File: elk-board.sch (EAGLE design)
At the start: 199 parts, among them IC1 KLM8G1GESD-B03P, IC10 MP2143DJ-LF-P, IC2 ALLWINNER--H3, IC3 SY6280, IC4 K4B4G1646D-BCK0, IC5 RT8059GJ5, IC6 RT8059GJ5, IC7 SY8089A, IC8 NCP803SN263T1G, IC9 RT8059GJ5, Q1 AO3415A, Q2 BCM856BS, Q3 9HT10-32.768KEZF-T, Q4 L2N7002WT1G, U1 AP6212, U2 STM32F411CEU6TR, X1 10118192-0001LF, Y1 26MHz, Y2 24MHz, Y3 CSTCW25M0X53-R0

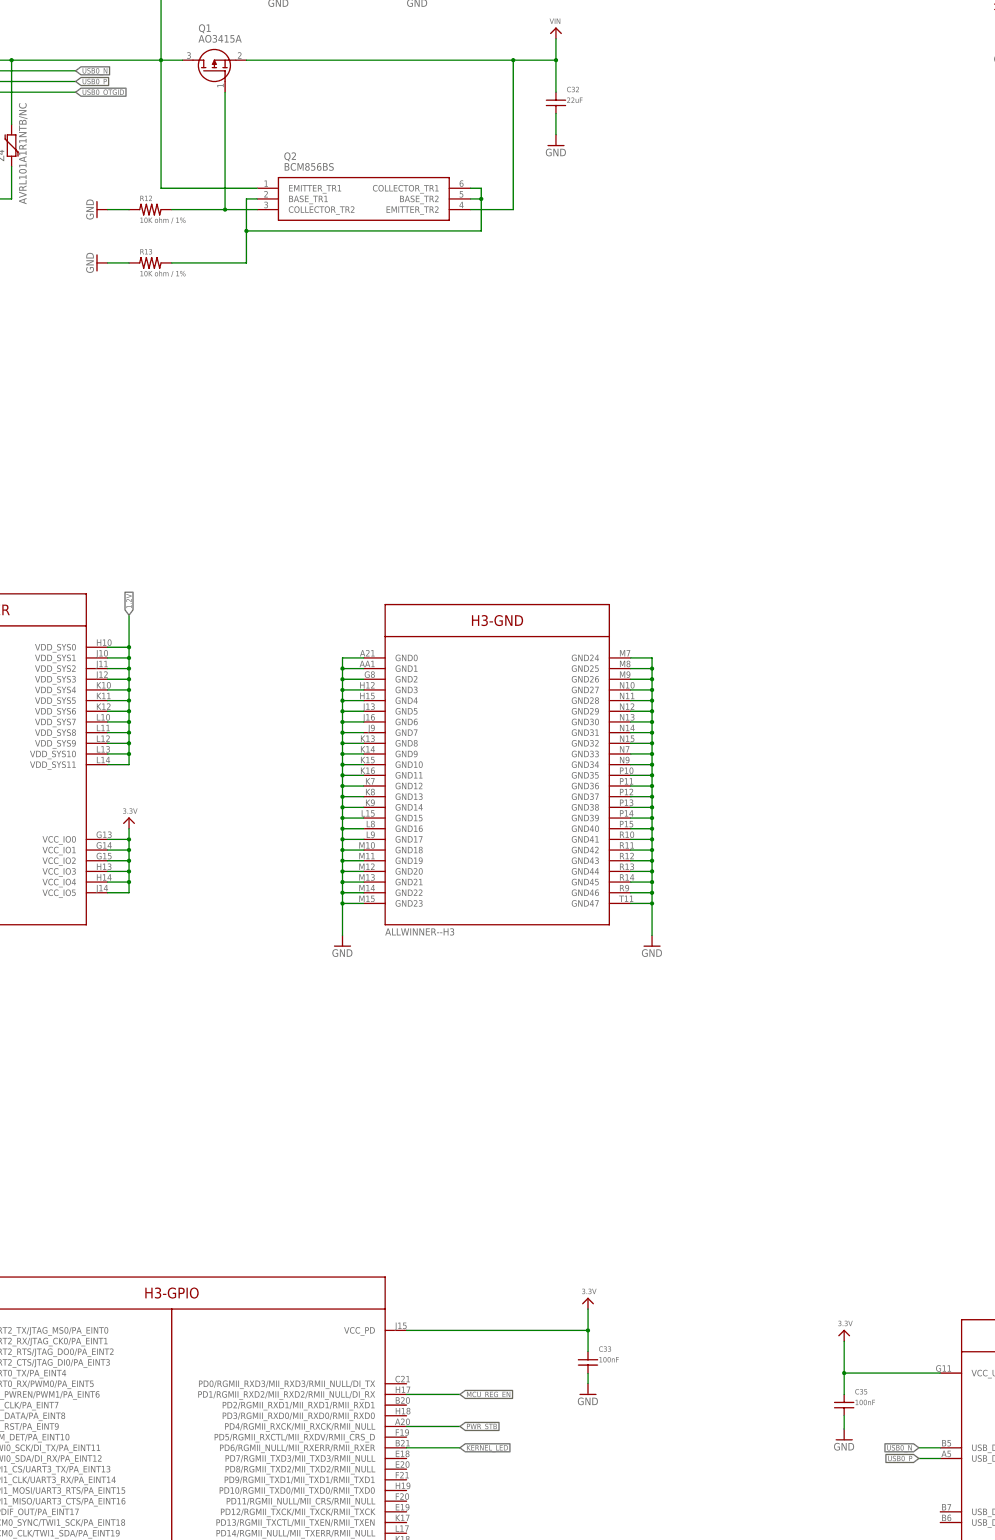
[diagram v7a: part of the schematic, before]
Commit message: Modified USB Diff Pair Impedence and Length Matching
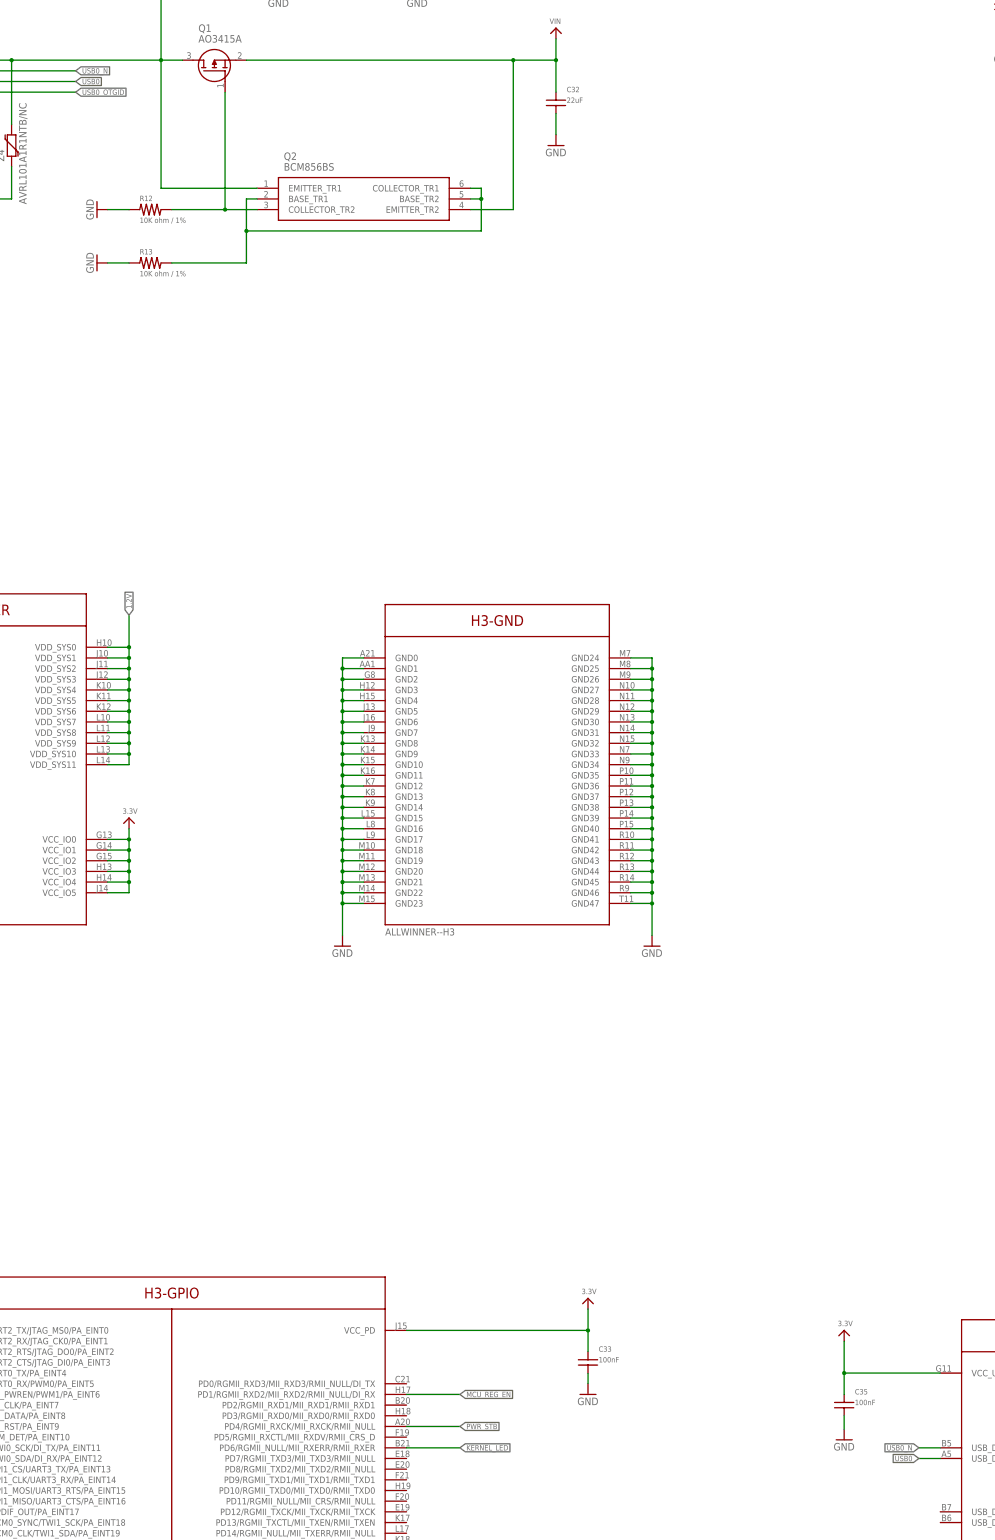
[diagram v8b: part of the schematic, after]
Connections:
- net USB0_P renamed USB0
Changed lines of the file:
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@@
 <clearance class="6" value="0.127"/>
 </class>
-<class number="7" name="DIFF90" width="0.115315625" drill="0">
+<class number="7" name="DIFF90" width="0.13461875" drill="0">
 <clearance class="0" value="0.3048"/>
 <clearance class="1" value="0.3048"/>
@@
 <clearance class="5" value="0.3048"/>
 <clearance class="6" value="0.3048"/>
+<clearance class="7" value="0.108965625"/>
 </class>
 <class number="8" name="SDC2" width="0" drill="0">
@@
 </segment>
 </net>
-<net name="USB0_P" class="7">
+<net name="USB0" class="7">
 <segment>
 <pinref part="IC2" gate="G$7" pin="USB_DP0"/>
